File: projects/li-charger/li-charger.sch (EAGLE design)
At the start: 23 parts, among them J1 Power Jack, Q1 IRF5305, Q2 BC547, Q3 BC327, Q4 BC337, U1 REG1117, U2 Arduino Pro Mini

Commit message: Update li-charger.sch
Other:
- note added: "Lithium-Ion Battery Charger"
- note removed: "Lithium Battery Charger"
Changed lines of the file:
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@@
 <wire x1="78.74" y1="-25.4" x2="78.74" y2="104.14" width="0.1524" layer="95"/>
 <wire x1="78.74" y1="104.14" x2="-55.88" y2="104.14" width="0.1524" layer="95"/>
-<text x="-48.26" y="-7.62" size="3.81" layer="95" align="top-left">Lithium Battery Charger</text>
-<text x="17.78" y="-7.62" size="2.1844" layer="95" align="top-left">Copyright © 2018, Karim Hraibi
+<text x="-48.26" y="-7.62" size="3.81" layer="95" align="top-left">Lithium-Ion Battery Charger</text>
+<text x="20.32" y="-7.62" size="2.1844" layer="95" align="top-left">Copyright © 2018, Karim Hraibi
 Please visit:
 www.microfarad.de

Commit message: Update li-charger.sch
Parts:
- removed Q3: BC327, transistor-pnp:BC327
- removed Q4: BC337, transistor-npn:BC337
- removed R3, R4: 10K, rcl:R-EU_0207/10
- R1, R2: value 10K -> 2K2
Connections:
- removed net N$4: R4.1, U2.8
- removed net N$6: Q3.B, R3.2
- removed net N$7: Q4.C, R3.1
- removed net N$8: Q4.B, R4.2
- removed net N$9: Q3.C, R5.2
- net 0V: no longer Q4.E
- net B+: now also R5.2; no longer Q3.E
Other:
- moved on the sheet: J2, J3, R2, R5, R6

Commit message: Updated schematic
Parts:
- added C5: 10µF Tantal, rcl:CPOL-EUE2.5-5
- added D2, D3, D4: 1N5819, diode:1N5819-B
- added D5: LED, SparkFun-LED:LED5MM
- added R3: 10K, rcl:R-EU_0207/10
- added R4: 180K, rcl:R-EU_0207/10
- C1: value 10µF Tantal -> 100µF; device rcl:C-EU025-040X050 -> rcl:CPOL-EUE2.5-5
- C2: value 10µF Tantal -> 330nF
- C3: value 10µF Tantal -> 100nF
- C4: device rcl:C-EU025-040X050 -> rcl:CPOL-EUE2.5-5
- D1: value LED -> 1N4004; device SparkFun-LED:LED5MM -> diode:1N4004
- R5: value 100K -> 10K
- R6: value 10K -> 2K2; device rcl:R-EU_0207/10 -> rcl:R-EU_0207/7
- R7: value 2K2 -> 10K; device rcl:R-EU_0207/7 -> rcl:R-EU_0207/10
- R8: value 10K -> 1R/3W; device rcl:R-EU_0207/10 -> rcl:R-EU_0617/22
- R9: value 0R5/3W -> 1R/3W
- U1: value REG1117 -> 7805; device burr-brown:REG1117 -> linear:7805TV
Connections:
- removed net +12V: C1.1, J1.PWR, Q1.S$1, R1.2, U1.VIN
- new net +29V: D1.A, J1.PWR, Q1.S$1, R1.2
- new net N$4: Q2.C, R2.1
- new net N$5: D2.A, D3.A, D4.A, Q1.D$1
- new net N$6: C1.+, C2.1, D1.C, U1.VI
- net +5V: now also C3.1, U1.VO; no longer C2.1, U1.VOUT
- net 0V: now also C1.-, C4.-, C5.-, D5.C, R7.1; no longer C1.2, C4.2, D1.C
- net B+: now also D2.C, D3.C, D4.C, R4.2; no longer Q1.D$1, R5.2
- net B-: now also R5.2, R8.2; no longer R6.2
- net N$1: now also R2.2; no longer Q2.C
- net N$10: now also C4.+, R4.1, R7.2; no longer C3.1, R5.1, R8.2
- net N$11: now also D5.A, R6.1; no longer D1.A, R7.1
- net N$12: now also R6.2; no longer R7.2
- net N$13: now also C5.+, R5.1; no longer C4.1, R6.1
- net N$2: now also R3.2; no longer R2.2
- net N$3: now also R3.1; no longer R2.1
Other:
- note added: "Copyright © 2019, Karim Hraibi Please visit: www.microfarad.de www.github.com/microfarad-de/li-charger"
- note removed: "Copyright © 2018, Karim Hraibi Please visit: www.microfarad.de www.github.com/microfarad-de/li-charger"
- moved on the sheet: C2, C3, Q2, R2, R5, R6, R7, R8, R9

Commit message: Update li-charger.sch
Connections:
- new net +19V: D1.A, J1.PWR
- net +29V: no longer D1.A, J1.PWR
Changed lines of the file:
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@@
 <part name="U2" library="microfarad-de" deviceset="ARDUINO_PRO_MINI" device="_TS" value="Arduino Pro Mini"/>
 <part name="P+2" library="supply1" library_urn="urn:adsk.eagle:library:371" deviceset="+5V" device=""/>
-<part name="P+1" library="supply1" library_urn="urn:adsk.eagle:library:371" deviceset="+12V" device="" value="+29V"/>
+<part name="P+1" library="supply1" library_urn="urn:adsk.eagle:library:371" deviceset="+12V" device="" value="+19V"/>
 <part name="C2" library="rcl" library_urn="urn:adsk.eagle:library:334" deviceset="C-EU" device="025-040X050" package3d_urn="urn:adsk.eagle:package:23634/1" value="330nF"/>
 <part name="R1" library="rcl" library_urn="urn:adsk.eagle:library:334" deviceset="R-EU_" device="0207/10" package3d_urn="urn:adsk.eagle:package:23491/2" value="2K2"/>
@@
 <part name="P+4" library="supply1" library_urn="urn:adsk.eagle:library:371" deviceset="+5V" device=""/>
 <part name="GND3" library="supply1" library_urn="urn:adsk.eagle:library:371" deviceset="0V" device=""/>
-<part name="P+3" library="supply1" library_urn="urn:adsk.eagle:library:371" deviceset="+12V" device="" value="+29V"/>
+<part name="P+3" library="supply1" library_urn="urn:adsk.eagle:library:371" deviceset="+12V" device="" value="+19V"/>
 <part name="R3" library="rcl" library_urn="urn:adsk.eagle:library:334" deviceset="R-EU_" device="0207/10" package3d_urn="urn:adsk.eagle:package:23491/2" value="10K"/>
 <part name="GND2" library="supply1" library_urn="urn:adsk.eagle:library:371" deviceset="0V" device=""/>
@@
 <junction x="58.42" y="88.9"/>
 </segment>
-<segment>
-<pinref part="J1" gate="G$1" pin="PWR"/>
-<pinref part="D1" gate="1" pin="A"/>
-<wire x1="-35.56" y1="81.28" x2="-33.02" y2="81.28" width="0.1524" layer="91"/>
-<pinref part="P+1" gate="1" pin="+12V"/>
-<wire x1="-33.02" y1="81.28" x2="-30.48" y2="81.28" width="0.1524" layer="91"/>
-<wire x1="-33.02" y1="91.44" x2="-33.02" y2="81.28" width="0.1524" layer="91"/>
-<junction x="-33.02" y="81.28"/>
-</segment>
 </net>
 <net name="0V" class="0">
@@
 </segment>
 </net>
+<net name="+19V" class="0">
+<segment>
+<pinref part="J1" gate="G$1" pin="PWR"/>
+<pinref part="D1" gate="1" pin="A"/>
+<wire x1="-35.56" y1="81.28" x2="-33.02" y2="81.28" width="0.1524" layer="91"/>
+<pinref part="P+1" gate="1" pin="+12V"/>
+<wire x1="-33.02" y1="81.28" x2="-30.48" y2="81.28" width="0.1524" layer="91"/>
+<wire x1="-33.02" y1="91.44" x2="-33.02" y2="81.28" width="0.1524" layer="91"/>
+<junction x="-33.02" y="81.28"/>
+</segment>
+</net>

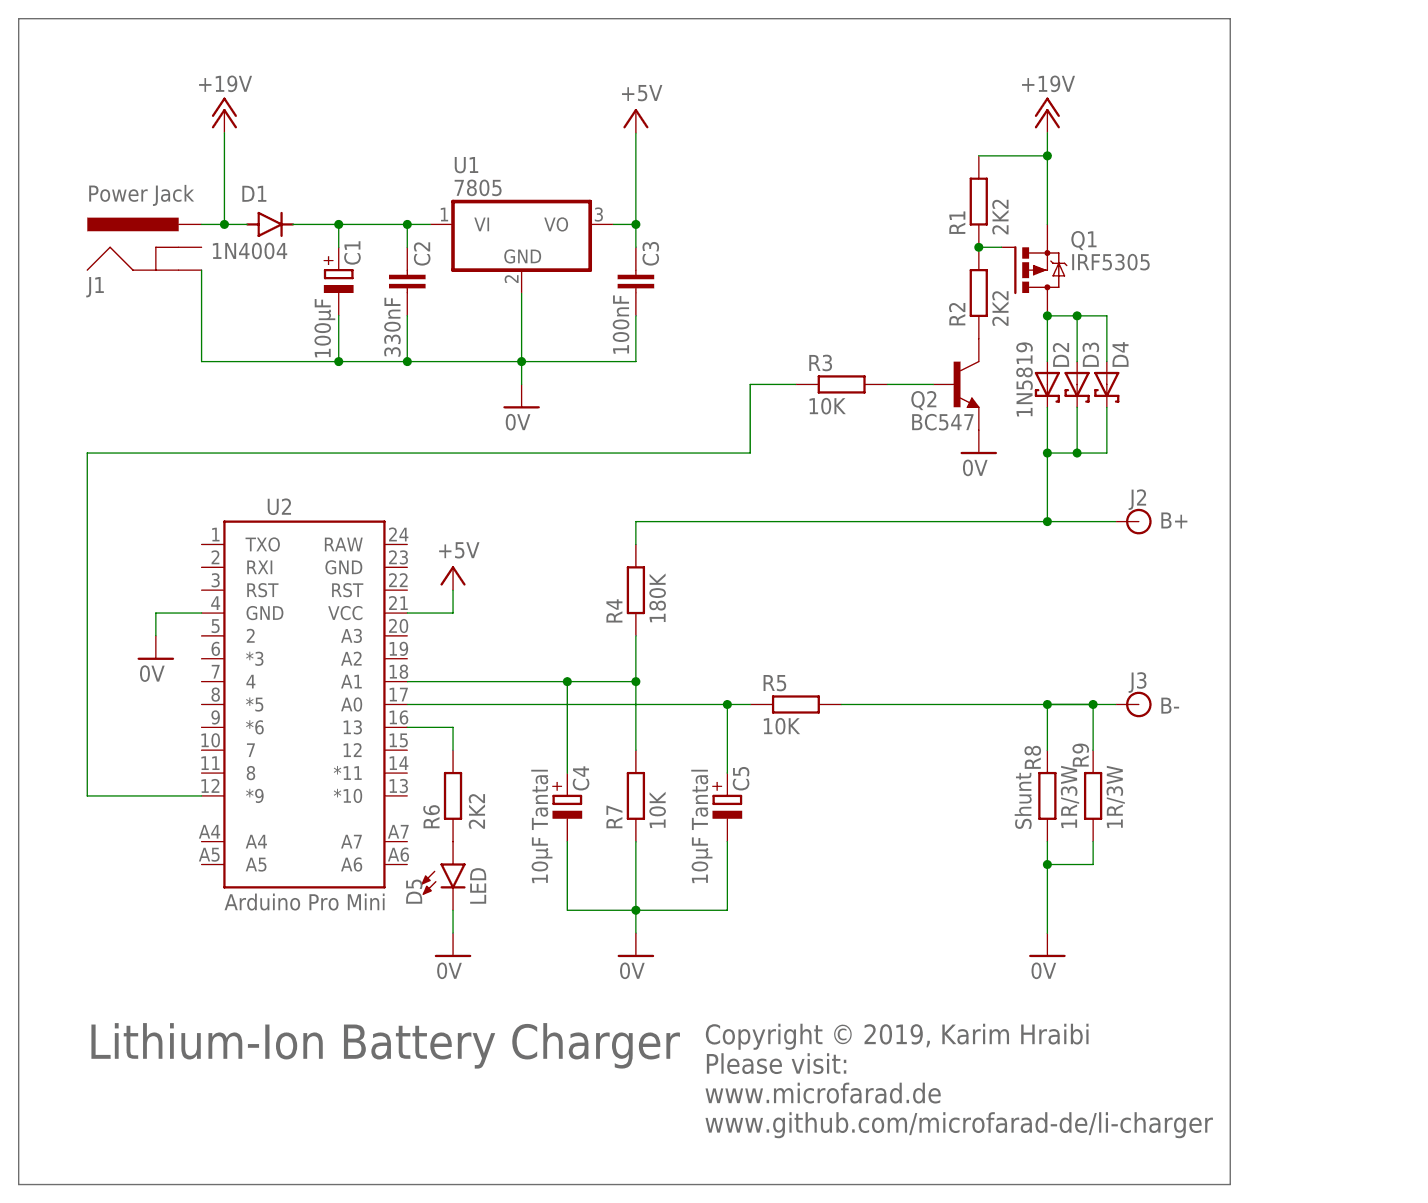
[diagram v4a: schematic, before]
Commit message: updated li-charger schematic
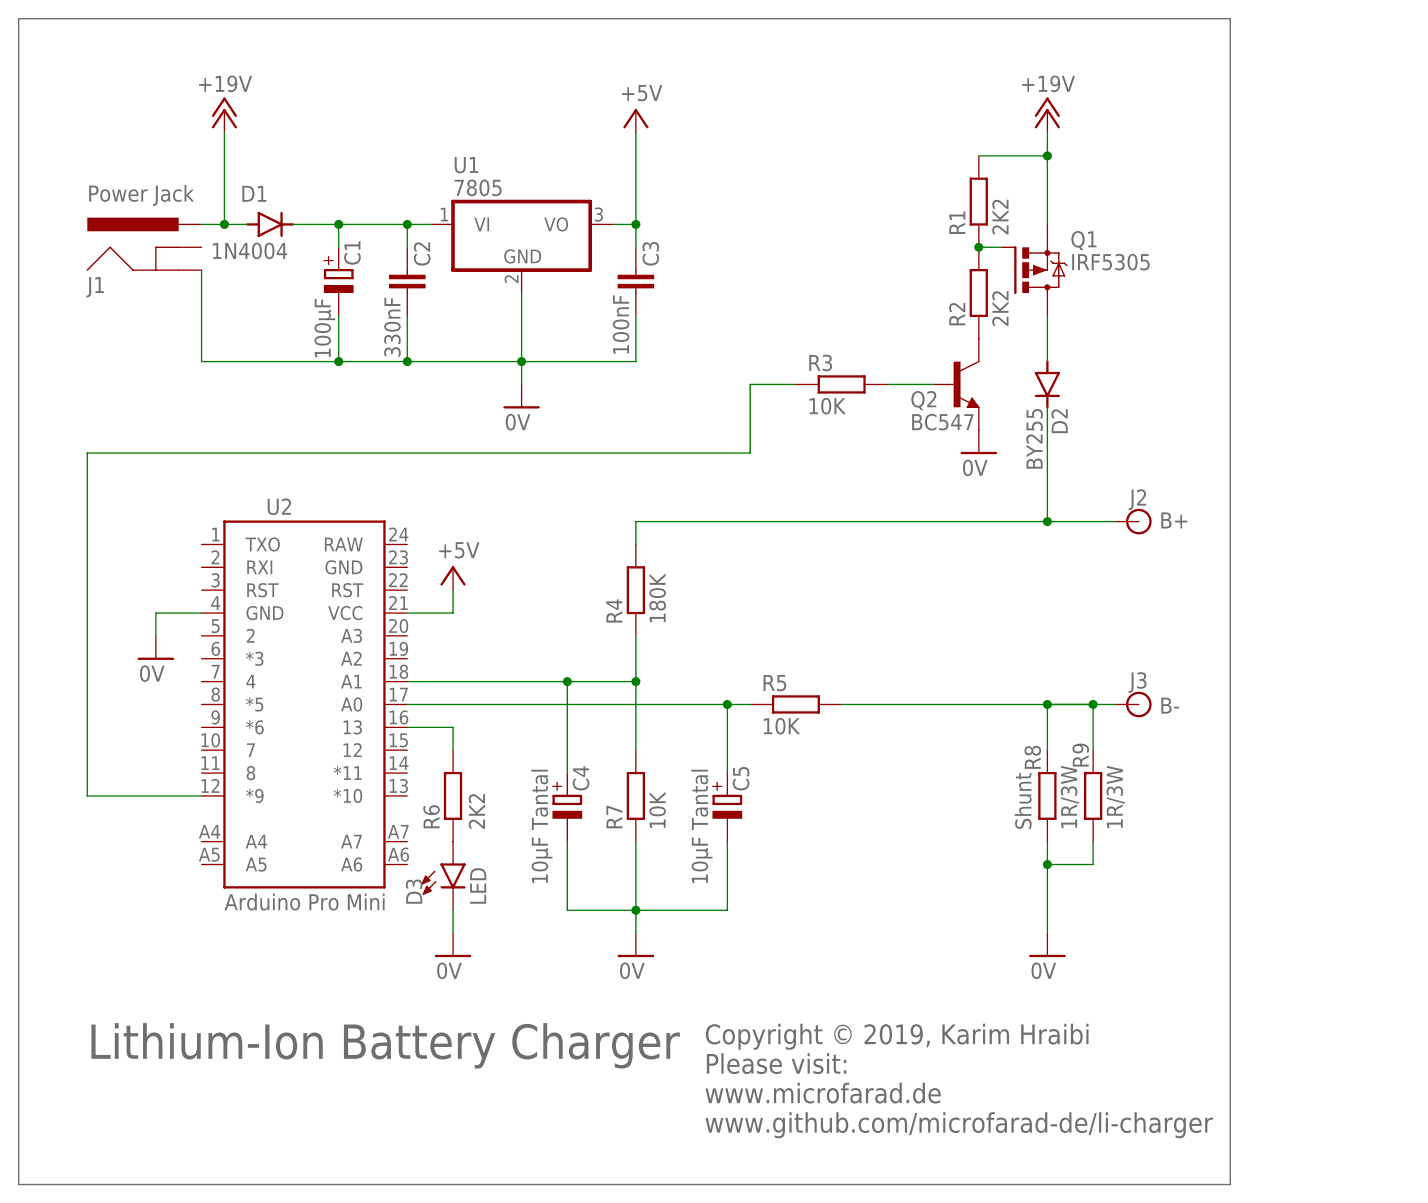
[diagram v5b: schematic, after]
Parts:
- removed D4: 1N5819, diode:1N5819-B
- removed D5: LED, SparkFun-LED:LED5MM
- D2: value 1N5819 -> BY255; device diode:1N5819-B -> diode:BY251
- D3: value 1N5819 -> LED; device diode:1N5819-B -> SparkFun-LED:LED5MM
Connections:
- net 0V: now also D3.C; no longer D5.C
- net B+: no longer D3.C, D4.C
- net N$11: now also D3.A; no longer D5.A
- net N$5: no longer D3.A, D4.A
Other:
- moved on the sheet: D3
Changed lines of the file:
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@@
 <part name="GND6" library="supply1" library_urn="urn:adsk.eagle:library:371" deviceset="0V" device=""/>
 <part name="R5" library="rcl" library_urn="urn:adsk.eagle:library:334" deviceset="R-EU_" device="0207/10" package3d_urn="urn:adsk.eagle:package:23491/2" value="10K"/>
-<part name="D5" library="SparkFun-LED" library_urn="urn:adsk.eagle:library:529" deviceset="LED" device="5MM" package3d_urn="urn:adsk.eagle:package:39353/1" value="LED"/>
+<part name="D3" library="SparkFun-LED" library_urn="urn:adsk.eagle:library:529" deviceset="LED" device="5MM" package3d_urn="urn:adsk.eagle:package:39353/1" value="LED"/>
 <part name="R6" library="rcl" library_urn="urn:adsk.eagle:library:334" deviceset="R-EU_" device="0207/7" package3d_urn="urn:adsk.eagle:package:23493/2" value="2K2"/>
 <part name="GND5" library="supply1" library_urn="urn:adsk.eagle:library:371" deviceset="0V" device=""/>
@@
 <part name="Q2" library="transistor-npn" library_urn="urn:adsk.eagle:library:398" deviceset="BC547*" device="" package3d_urn="urn:adsk.eagle:package:28523/2"/>
 <part name="R2" library="rcl" library_urn="urn:adsk.eagle:library:334" deviceset="R-EU_" device="0207/10" package3d_urn="urn:adsk.eagle:package:23491/2" value="2K2"/>
-<part name="D2" library="diode" library_urn="urn:adsk.eagle:library:210" deviceset="1N581*" device="" package3d_urn="urn:adsk.eagle:package:43421/1" technology="9-B" value="1N5819"/>
-<part name="D3" library="diode" library_urn="urn:adsk.eagle:library:210" deviceset="1N581*" device="" package3d_urn="urn:adsk.eagle:package:43421/1" technology="9-B" value="1N5819"/>
-<part name="D4" library="diode" library_urn="urn:adsk.eagle:library:210" deviceset="1N581*" device="" package3d_urn="urn:adsk.eagle:package:43421/1" technology="9-B" value="1N5819"/>
 <part name="D1" library="diode" library_urn="urn:adsk.eagle:library:210" deviceset="1N4004" device="" package3d_urn="urn:adsk.eagle:package:43336/1"/>
 <part name="U1" library="linear" library_urn="urn:adsk.eagle:library:262" deviceset="78*" device="TV" package3d_urn="urn:adsk.eagle:package:16417/1" technology="05" value="7805"/>
@@
 <part name="C5" library="rcl" library_urn="urn:adsk.eagle:library:334" deviceset="CPOL-EU" device="E2.5-5" package3d_urn="urn:adsk.eagle:package:23344/1" value="10µF Tantal"/>
 <part name="R9" library="rcl" library_urn="urn:adsk.eagle:library:334" deviceset="R-EU_" device="0617/22" package3d_urn="urn:adsk.eagle:package:23577/1" value="1R/3W"/>
+<part name="D2" library="diode" library_urn="urn:adsk.eagle:library:210" deviceset="BY251" device="" package3d_urn="urn:adsk.eagle:package:43365/1" value="BY255"/>
 </parts>
 <sheets>
@@
 <attribute name="VALUE" x="26.67" y="24.638" size="1.778" layer="96"/>
 </instance>
-<instance part="D5" gate="G$1" x="-7.62" y="10.16" smashed="yes">
+<instance part="D3" gate="G$1" x="-7.62" y="10.16" smashed="yes">
 <attribute name="NAME" x="-11.049" y="5.588" size="1.778" layer="95" rot="R90"/>
 <attribute name="VALUE" x="-5.715" y="5.588" size="1.778" layer="96" rot="R90" align="top-left"/>
@@
 <attribute name="VALUE" x="54.102" y="69.85" size="1.778" layer="96" rot="R90"/>
 </instance>
-<instance part="D2" gate="G$1" x="58.42" y="63.5" smashed="yes" rot="R270">
-<attribute name="NAME" x="59.055" y="68.326" size="1.778" layer="95" rot="R270"/>
-<attribute name="VALUE" x="54.991" y="68.326" size="1.778" layer="96" rot="R270"/>
-</instance>
-<instance part="D3" gate="G$1" x="61.722" y="63.5" smashed="yes" rot="R270">
-<attribute name="NAME" x="62.357" y="68.326" size="1.778" layer="95" rot="R270"/>
-</instance>
-<instance part="D4" gate="G$1" x="65.024" y="63.5" smashed="yes" rot="R270">
-<attribute name="NAME" x="65.659" y="68.326" size="1.778" layer="95" rot="R270"/>
-</instance>
 <instance part="D1" gate="1" x="-27.94" y="81.28" smashed="yes">
 <attribute name="NAME" x="-31.242" y="83.7946" size="1.778" layer="95"/>
@@
 <attribute name="NAME" x="63.0174" y="20.828" size="1.778" layer="95" rot="R90"/>
 <attribute name="VALUE" x="66.802" y="13.97" size="1.778" layer="96" rot="R90"/>
+</instance>
+<instance part="D2" gate="1" x="58.42" y="63.5" smashed="yes" rot="R270">
+<attribute name="NAME" x="58.9026" y="60.96" size="1.778" layer="95" rot="R270"/>
+<attribute name="VALUE" x="56.1086" y="60.96" size="1.778" layer="96" rot="R270"/>
 </instance>
 </instances>
@@
 </segment>
 <segment>
-<pinref part="D5" gate="G$1" pin="C"/>
+<pinref part="D3" gate="G$1" pin="C"/>
 <wire x1="-7.62" y1="5.08" x2="-7.62" y2="2.54" width="0.1524" layer="91"/>
 <pinref part="GND5" gate="1" pin="0V"/>
@@
 <wire x1="58.42" y1="48.26" x2="12.7" y2="48.26" width="0.1524" layer="91"/>
 <wire x1="12.7" y1="48.26" x2="12.7" y2="45.72" width="0.1524" layer="91"/>
-<pinref part="D2" gate="G$1" pin="C"/>
-<wire x1="58.42" y1="60.96" x2="58.42" y2="55.88" width="0.1524" layer="91"/>
 <junction x="58.42" y="48.26"/>
-<pinref part="D3" gate="G$1" pin="C"/>
-<wire x1="58.42" y1="55.88" x2="58.42" y2="48.26" width="0.1524" layer="91"/>
-<wire x1="61.722" y1="60.96" x2="61.722" y2="55.88" width="0.1524" layer="91"/>
-<wire x1="61.722" y1="55.88" x2="58.42" y2="55.88" width="0.1524" layer="91"/>
-<junction x="58.42" y="55.88"/>
-<pinref part="D4" gate="G$1" pin="C"/>
-<wire x1="65.024" y1="60.96" x2="65.024" y2="55.88" width="0.1524" layer="91"/>
-<wire x1="65.024" y1="55.88" x2="61.722" y2="55.88" width="0.1524" layer="91"/>
-<junction x="61.722" y="55.88"/>
+<wire x1="58.42" y1="60.96" x2="58.42" y2="48.26" width="0.1524" layer="91"/>
+<pinref part="D2" gate="1" pin="C"/>
 </segment>
 </net>
@@
 <net name="N$11" class="0">
 <segment>
-<pinref part="D5" gate="G$1" pin="A"/>
+<pinref part="D3" gate="G$1" pin="A"/>
 <pinref part="R6" gate="G$1" pin="1"/>
 </segment>
@@
 <pinref part="Q2" gate="G$1" pin="C"/>
 <pinref part="R2" gate="G$1" pin="1"/>
-</segment>
-</net>
-<net name="N$5" class="0">
-<segment>
-<pinref part="D2" gate="G$1" pin="A"/>
-<pinref part="Q1" gate="G$1" pin="D$1"/>
-<wire x1="58.42" y1="66.04" x2="58.42" y2="71.12" width="0.1524" layer="91"/>
-<pinref part="D3" gate="G$1" pin="A"/>
-<wire x1="58.42" y1="71.12" x2="61.722" y2="71.12" width="0.1524" layer="91"/>
-<wire x1="61.722" y1="71.12" x2="61.722" y2="66.04" width="0.1524" layer="91"/>
-<junction x="58.42" y="71.12"/>
-<pinref part="D4" gate="G$1" pin="A"/>
-<wire x1="61.722" y1="71.12" x2="65.024" y2="71.12" width="0.1524" layer="91"/>
-<wire x1="65.024" y1="71.12" x2="65.024" y2="66.04" width="0.1524" layer="91"/>
-<junction x="61.722" y="71.12"/>
 </segment>
 </net>
@@
 </segment>
 </net>
+<net name="N$5" class="0">
+<segment>
+<pinref part="Q1" gate="G$1" pin="D$1"/>
+<pinref part="D2" gate="1" pin="A"/>
+<wire x1="58.42" y1="71.12" x2="58.42" y2="66.04" width="0.1524" layer="91"/>
+</segment>
+</net>

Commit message: updated schematic
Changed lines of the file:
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@@
 <part name="U2" library="microfarad-de" deviceset="ARDUINO_PRO_MINI" device="_TS" value="Arduino Pro Mini"/>
 <part name="P+2" library="supply1" library_urn="urn:adsk.eagle:library:371" deviceset="+5V" device=""/>
-<part name="P+1" library="supply1" library_urn="urn:adsk.eagle:library:371" deviceset="+12V" device="" value="+19V"/>
+<part name="P+1" library="supply1" library_urn="urn:adsk.eagle:library:371" deviceset="+12V" device="" value="+19.5V"/>
 <part name="C2" library="rcl" library_urn="urn:adsk.eagle:library:334" deviceset="C-EU" device="025-040X050" package3d_urn="urn:adsk.eagle:package:23634/1" value="330nF"/>
 <part name="R1" library="rcl" library_urn="urn:adsk.eagle:library:334" deviceset="R-EU_" device="0207/10" package3d_urn="urn:adsk.eagle:package:23491/2" value="2K2"/>
@@
 <part name="P+4" library="supply1" library_urn="urn:adsk.eagle:library:371" deviceset="+5V" device=""/>
 <part name="GND3" library="supply1" library_urn="urn:adsk.eagle:library:371" deviceset="0V" device=""/>
-<part name="P+3" library="supply1" library_urn="urn:adsk.eagle:library:371" deviceset="+12V" device="" value="+19V"/>
+<part name="P+3" library="supply1" library_urn="urn:adsk.eagle:library:371" deviceset="+12V" device="" value="+19.5V"/>
 <part name="R3" library="rcl" library_urn="urn:adsk.eagle:library:334" deviceset="R-EU_" device="0207/10" package3d_urn="urn:adsk.eagle:package:23491/2" value="10K"/>
 <part name="GND2" library="supply1" library_urn="urn:adsk.eagle:library:371" deviceset="0V" device=""/>
